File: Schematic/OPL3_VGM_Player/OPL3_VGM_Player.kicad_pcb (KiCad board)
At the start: 2 copper layers, 10.6 x 6 mm, 54 parts, among them J1 USB_OTG, J2 Conn_02x03_Odd_Even, J3 Micro_SD_Card, J4 Conn_01x04, J5 Audio-Jack-3, SW1 SW_Push_Dual, SW2 SW_Push_Dual, SW3 SW_Push_Dual, SW4 SW_Push_Dual, SW5 SW_Push_Dual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

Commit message: PCB first pass
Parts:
- added H1: M3, Mounting_Holes:MountingHole_3.2mm_M3, F.Cu at (226.1, 137.2)
- added H2: M3, Mounting_Holes:MountingHole_3.2mm_M3, F.Cu at (153.7, 137.2)
- added H3: M3, Mounting_Holes:MountingHole_3.2mm_M3, F.Cu at (153.7, 87.6)
- added H4: M3, Mounting_Holes:MountingHole_3.2mm_M3, F.Cu at (226.1, 87.6)
- moved RV1 87.6 mm to (224.2, 99.1)
- moved DS1 76.8 mm to (186.1, 129.5)
- moved J5 73.5 mm to (212.7, 91.4), turned to 180 degrees
- moved SW2 72.5 mm to (158.1, 129.9)
- moved C13 68.2 mm to (209.6, 101.6)
- moved C16 64.3 mm to (215.7, 115.3), turned to 90 degrees
- moved SW4 57.8 mm to (176.5, 129.9)
- moved U3 51.5 mm to (186.9, 102.9), turned to 270 degrees
- moved C22 50.3 mm to (222.9, 104.8), turned to 90 degrees
- moved C17 47.8 mm to (224.7, 110.9), turned to 270 degrees
- moved C23 45.4 mm to (226.7, 104.8), turned to 90 degrees
- moved C19 45.3 mm to (216.3, 120.1)
- moved R7 43.2 mm to (179.9, 121.5), turned to 180 degrees
- moved U5 42.8 mm to (208.5, 113.4)
- moved U4 42.4 mm to (197.1, 114.5)
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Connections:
- J1 pad 6: Net-(J1-Pad6) -> (no net)
- J5 pad 1: Net-(J5-Pad1) -> GND
- J5 pad 3: GND -> Net-(J5-Pad3)
- RV1 pad 2: Net-(J5-Pad1) -> Net-(J5-Pad3)
- U3 pad 7: VCC -> +5V
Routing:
- net +3V3: track 0.00 -> 133.0 mm, vias 0 -> 5
- net VCC: track 0.00 -> 64.6 mm
- net OPTION: track 0.00 -> 61.8 mm, vias 0 -> 5
- net GND: track 0.00 -> 50.8 mm, vias 0 -> 80
- net D2: track 0.00 -> 42.7 mm, vias 0 -> 2
- net YM_CLK: track 0.00 -> 41.6 mm, vias 0 -> 2
- net +5VA: track 0.00 -> 41.4 mm
- net NEXT: track 0.00 -> 40.1 mm, vias 0 -> 4
- net SWDIO: track 0.00 -> 39.5 mm, vias 0 -> 1
- net SCL: track 0.00 -> 34.3 mm, vias 0 -> 2
- net +5V: track 0.00 -> 33.4 mm
- net Net-(R2-Pad1): track 0.00 -> 32.3 mm, vias 0 -> 2
- net YM_A1: track 0.00 -> 32.1 mm, vias 0 -> 4
- net SDA: track 0.00 -> 30.9 mm, vias 0 -> 2
- net Net-(C18-Pad2): track 0.00 -> 29.5 mm, vias 0 -> 2
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- added copper zone on B.Cu, net GND
- added copper zone on F.Cu, net GND
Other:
- board size 10.6 x 6 mm -> 80 x 57.2 mm
- net class 3.3 added: clearance 0.2, trace_width 0.25, via_dia 0.8, via_drill 0.4
- net class 5v added: clearance 0.2, trace_width 0.4, via_dia 0.8, via_drill 0.4

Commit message: PCB first pass
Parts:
- renumbered SW4 to NEXT, SW5 to PLAYMODE, SW2 to PREV, SW3 to RAND, SW1 to RESET
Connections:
- U6 pad 11: Net-(U6-Pad11) -> GND
- U6 pad 4: Net-(U6-Pad4) -> +5VA
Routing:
- net +5VA: track 41.4 -> 52.2 mm
- net GND: track 50.8 -> 52.7 mm, vias 80 -> 81

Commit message: PCB Complete
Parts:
- added G***: LOGO, art:LOGO_1, F.Cu at (205.7, 138.4)
- added G***: LOGO, art:OPL3_LOGO, F.Cu at (200.0, 99.1)
- added G***: LOGO, art:VOICE_LOGO, B.Cu at (190.5, 113.0)
- moved DS1 0.41 mm to (185.6, 129.5)
- moved L3 0.41 mm to (183.8, 127.0)
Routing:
- net Net-(C23-Pad2): track 9.84 -> 14.8 mm
- net Net-(C22-Pad2): track 4.74 -> 9.74 mm
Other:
- board text added: "2019"
- board text added: "2019 Aidan Lawrence www.aidanlawrence.com"
- board text added: "3.3V"
- board text added: "B0"
- board text added: "B1"
- board text added: "GND"
- board text added: "SWC"
- board text added: "SWD"
- board text added: "V1"
- board text added: "www.aidanlawrence.com"

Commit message: Minor change to headphone jack
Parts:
- J5: footprint 35RAPC4BHN2:SWITCHCRAFT_35RAPC4BHN2 -> Boom Precision Elec PJ-307C:Boom Precision Elec PJ-307C
- moved J5 3.14 mm to (212.7, 88.3)
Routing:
- net Net-(J5-Pad3): track 6.98 -> 8.58 mm
- net Net-(J5-Pad2): track 15.2 -> 16.1 mm
- net GND: vias 81 -> 82
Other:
- board text added: "JLCJLCJLCJLC"
- board text added: "V2"
- board text removed: "V1"

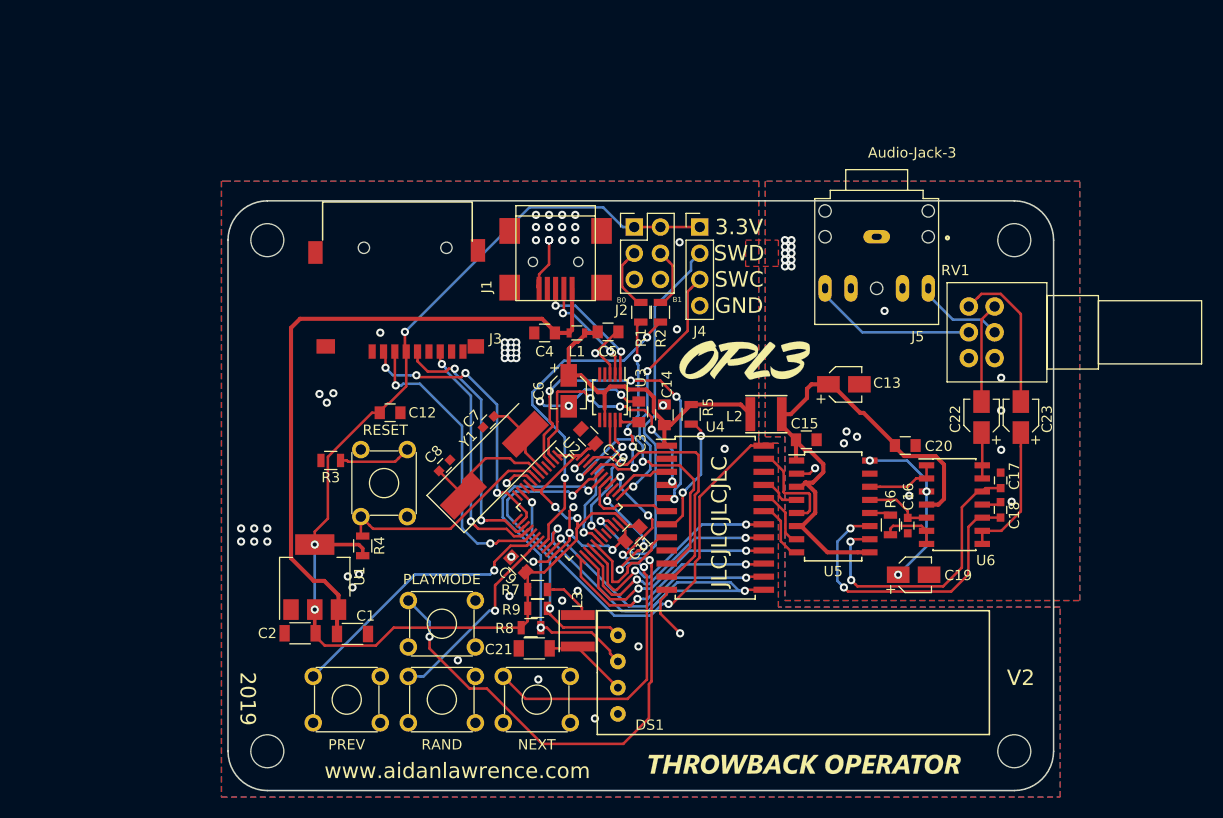
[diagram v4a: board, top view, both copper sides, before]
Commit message: SMD caps and fixed headphone jack pin sizes
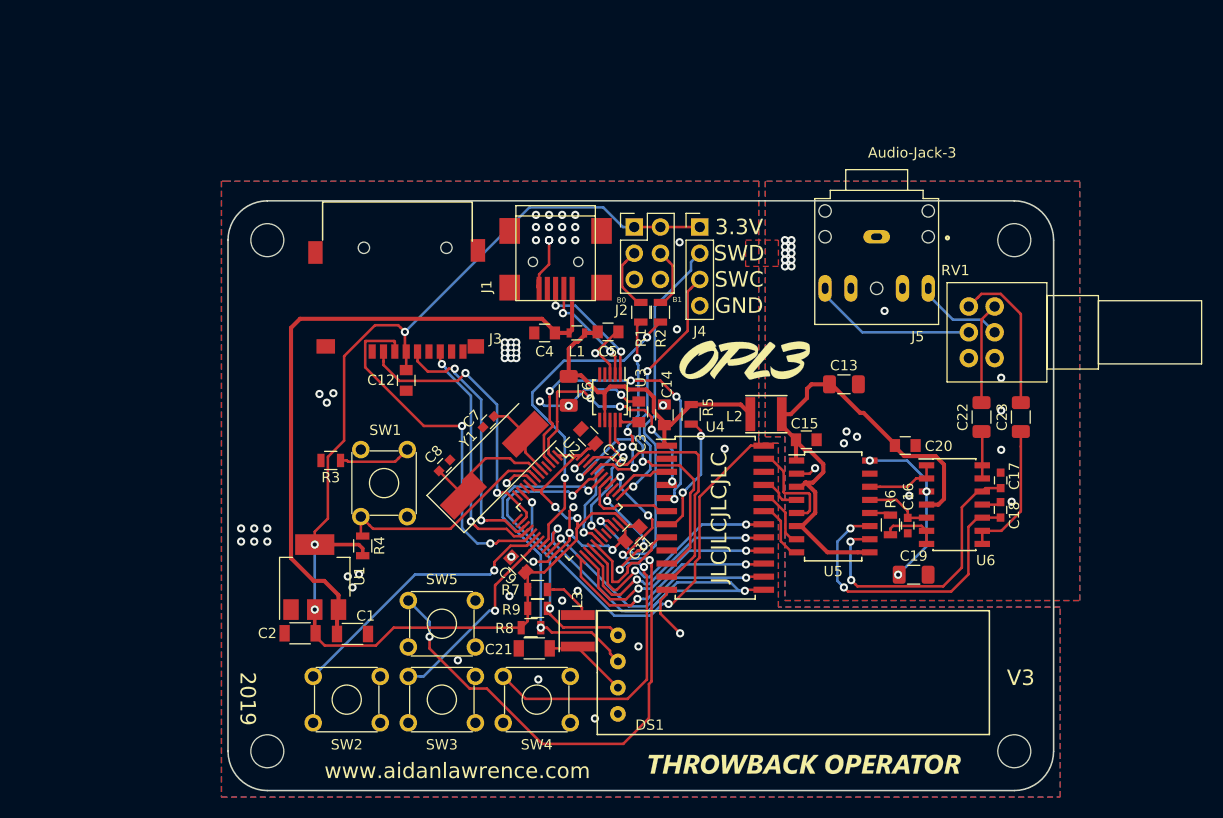
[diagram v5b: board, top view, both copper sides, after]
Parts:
- C13, C19, C22, C23, C6: footprint Capacitors_SMD:CP_Elec_3x5.3 -> Capacitor_SMD:C_1206_3216Metric
- moved C12 3.50 mm to (167.1, 101.2), turned to 270 degrees
- renumbered RESET to SW1, PREV to SW2, RAND to SW3, NEXT to SW4, PLAYMODE to SW5
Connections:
- J1 pad 6: (no net) -> Net-(J1-Pad6)
- U6 pad 11: GND -> Net-(U6-Pad11)
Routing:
- net SD_MOSI: track 29.2 -> 35.8 mm
- net +3V3: track 133.0 -> 138.8 mm
- net SD_CS: track 27.7 -> 28.2 mm, vias 4 -> 2
- net GND: vias 82 -> 81
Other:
- board text added: "V3"
- board text removed: "V2"
